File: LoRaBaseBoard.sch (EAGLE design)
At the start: 7 parts

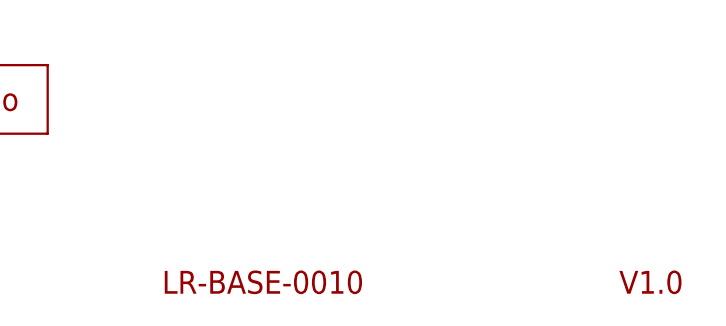
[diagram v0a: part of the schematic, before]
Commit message: Fixed fill distance. Generated CAM files. Generated PNG preview.
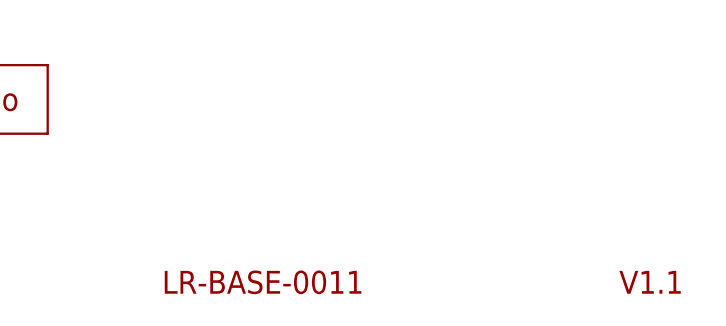
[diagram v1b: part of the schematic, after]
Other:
- note added: "LR-BASE-0011"
- note added: "V1.1"
- note removed: "LR-BASE-0010"
- note removed: "V1.0"
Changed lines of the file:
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@@
 <sheet>
 <plain>
-<text x="254" y="7.62" size="2.54" layer="94">V1.0</text>
-<text x="203.2" y="7.62" size="2.54" layer="94">LR-BASE-0010</text>
+<text x="254" y="7.62" size="2.54" layer="94">V1.1</text>
+<text x="203.2" y="7.62" size="2.54" layer="94">LR-BASE-0011</text>
 </plain>
 <instances>
